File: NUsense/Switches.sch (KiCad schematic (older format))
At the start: 21 parts, among them Q401 2N3055, SW401 SW_SPST, U401 ADM6713RAKS

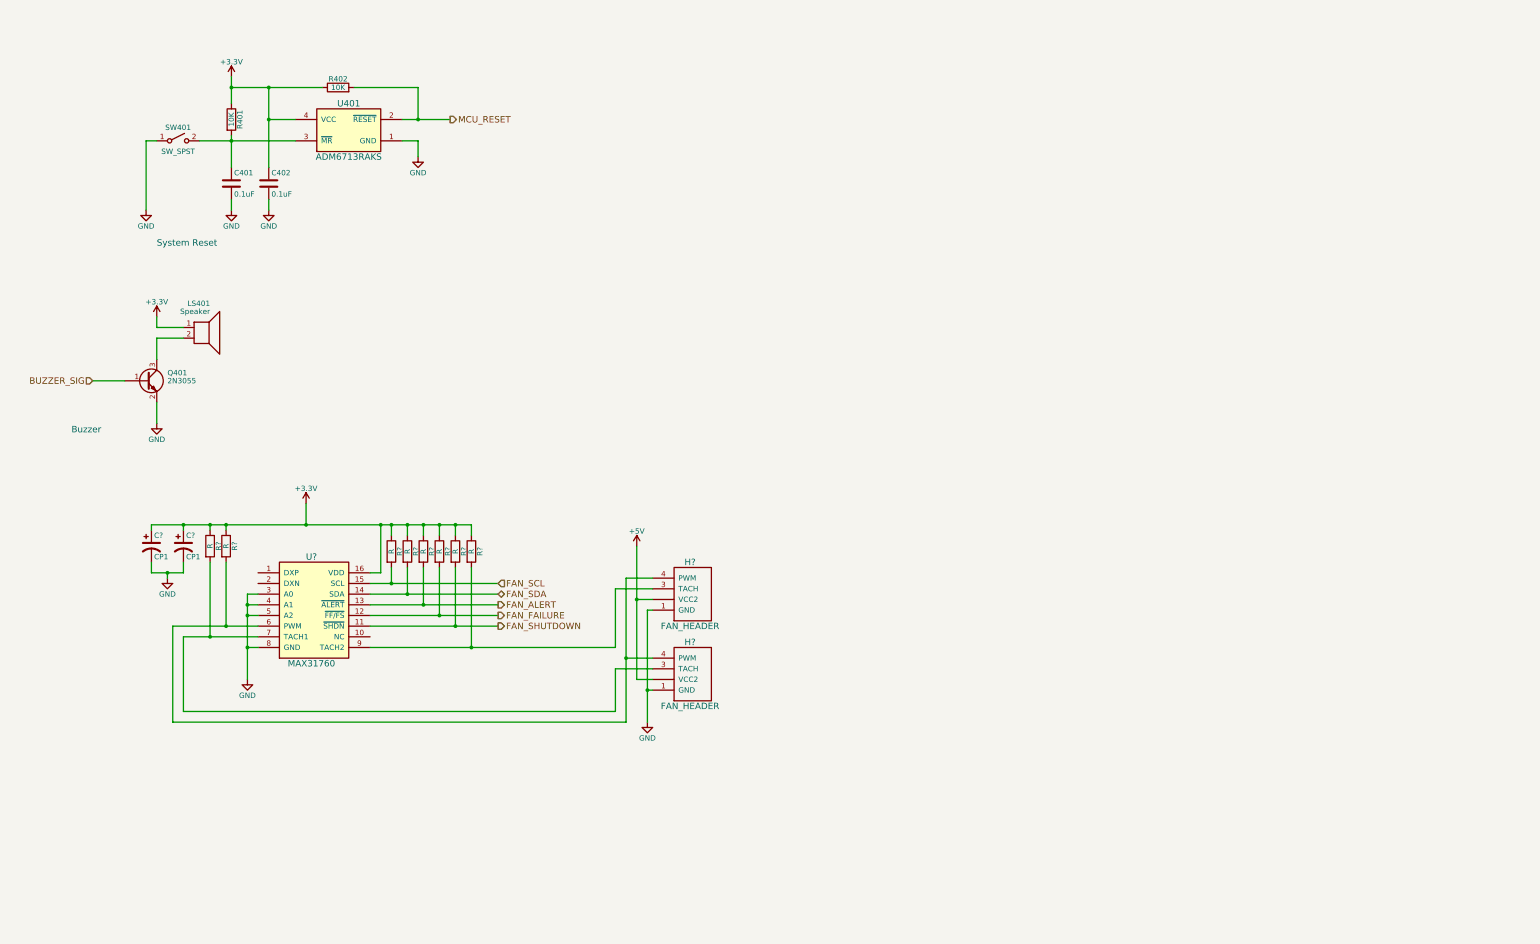
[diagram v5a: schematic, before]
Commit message: Add LED and Button
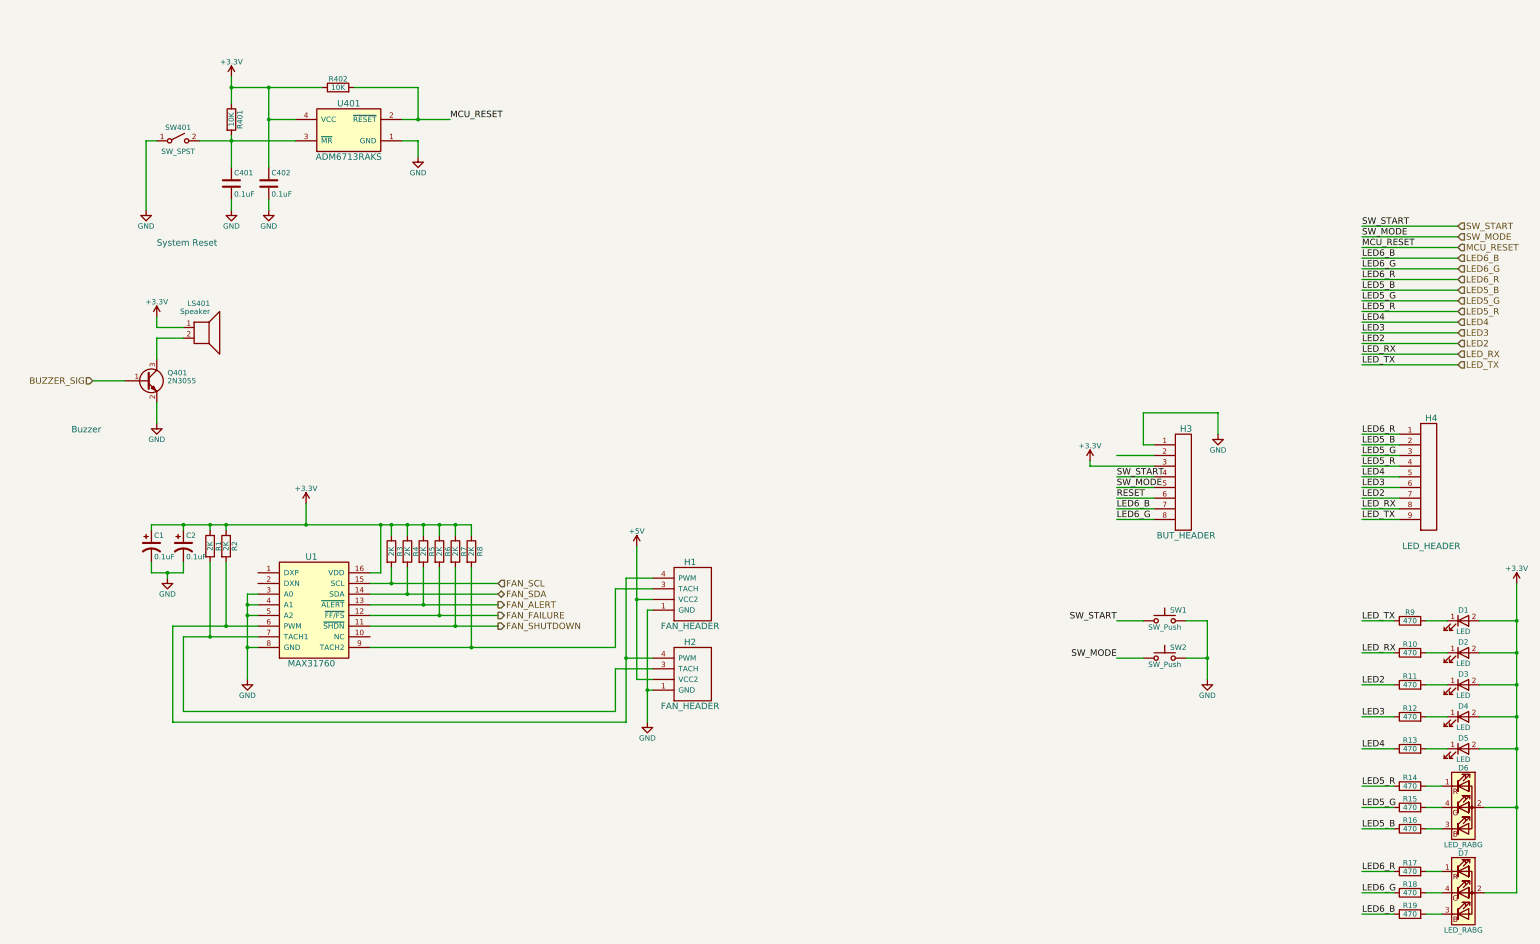
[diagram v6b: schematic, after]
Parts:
- removed R? (x7): R, symbol R
- added D1, D2, D3, D4, D5: LED, symbol LED
- added D6, D7: LED_RABG, symbol LED_RABG
- added H3: BUT_HEADER, symbol BUT_HEADER
- added H4: LED_HEADER, symbol LED_HEADER
- added R1, R2, R4, R5, R6, R7, R8: 2K, symbol R
- added R10, R11, R12, R13, R14, R15, R16, R17, R18, R19, R9: 470, Resistors_SMD:R_0805_HandSoldering, symbol R
- added SW1, SW2: SW_Push, symbol SW_Push
- C1, C2: renamed from C?; value CP1 -> 0.1uF
- R3: renamed from R?; value R -> 2K
- gave numbers to parts that had none: 3
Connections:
- net +3V3: now also D1.2 (A), D2.2 (A), D3.2 (A), D4.2 (A), D5.2 (A), D6.2 (A), D7.2 (A), H3.3, R1.1, R2.1, R4.1, R5.1, R6.1, R7.1, R8.1
- net FAN_ALERT: now also R5.2
- net FAN_FAILURE: now also R6.2
- net FAN_SDA: now also R4.2
- net FAN_SHUTDOWN: now also R7.2
- net GND: now also H3.1, SW1.2, SW2.2
- net at H1.4 (PWM), H2.4 (PWM), U1.6 (PWM): now also R2.2
- net at H2.3 (TACH), U1.7 (TACH1): now also R1.2
- net at H1.3 (TACH), U1.9 (TACH2): now also R8.2
- new net: D1.1 (K), R9.2
- new net: D2.1 (K), R10.2
- new net: D3.1 (K), R11.2
- new net: D4.1 (K), R12.2
- new net: D5.1 (K), R13.2
- new net: D6.1 (RK), R14.2
- new net: D6.3 (BK), R16.2
- new net: D6.4 (GK), R15.2
- new net: D7.1 (RK), R17.2
- new net: D7.3 (BK), R19.2
- new net: D7.4 (GK), R18.2
- new net LED2: H4.7, R11.1
- new net LED3: H4.6, R12.1
- new net LED4: H4.5, R13.1
- new net LED5_B: H4.2, R16.1
- new net LED5_G: H4.3, R15.1
- new net LED5_R: H4.4, R14.1
- new net LED6_B: H3.7, R19.1
- new net LED6_G: H3.8, R18.1
- new net LED6_R: H4.1, R17.1
- new net LED_RX: H4.8, R10.1
- new net LED_TX: H4.9, R9.1
- new net RESET: H3.6
- new net SW_MODE: H3.5, SW2.1
- new net SW_START: H3.4, SW1.1

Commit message: Cleans up some minor things
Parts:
- added C401, C402: 100nF, symbol C
- renumbered C401 to C403, C402 to C404, C1 to C405, C2 to C406, D1 to D401, D2 to D402, D3 to D403, D4 to D404, D5 to D405, D6 to D406, D7 to D407, H3 to H401, H1 to H402, H2 to H403, H4 to H404, R9 to R403, R10 to R404, R11 to R405, R12 to R406, R13 to R407, R14 to R408, R15 to R409, R16 to R410, R17 to R411, R18 to R412, R19 to R413, R1 to R414, R2 to R415, R3 to R416, R4 to R417, R5 to R418, R6 to R419, R7 to R420, R8 to R421, SW1 to SW402, SW2 to SW403, U1 to U402
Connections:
- net RESET is gone; now on net MCU_RESET: H401.6
- net GND: now also C401.2, C402.2
- net SW_MODE: now also C402.1
- net SW_START: now also C401.1
- no-connect marks 0 -> 1
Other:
- moved on the sheet: C403, C404, C405, C406, D401, D402, D403, D404, D405, D406, D407, H401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
